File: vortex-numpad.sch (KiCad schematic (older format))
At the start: 16 parts

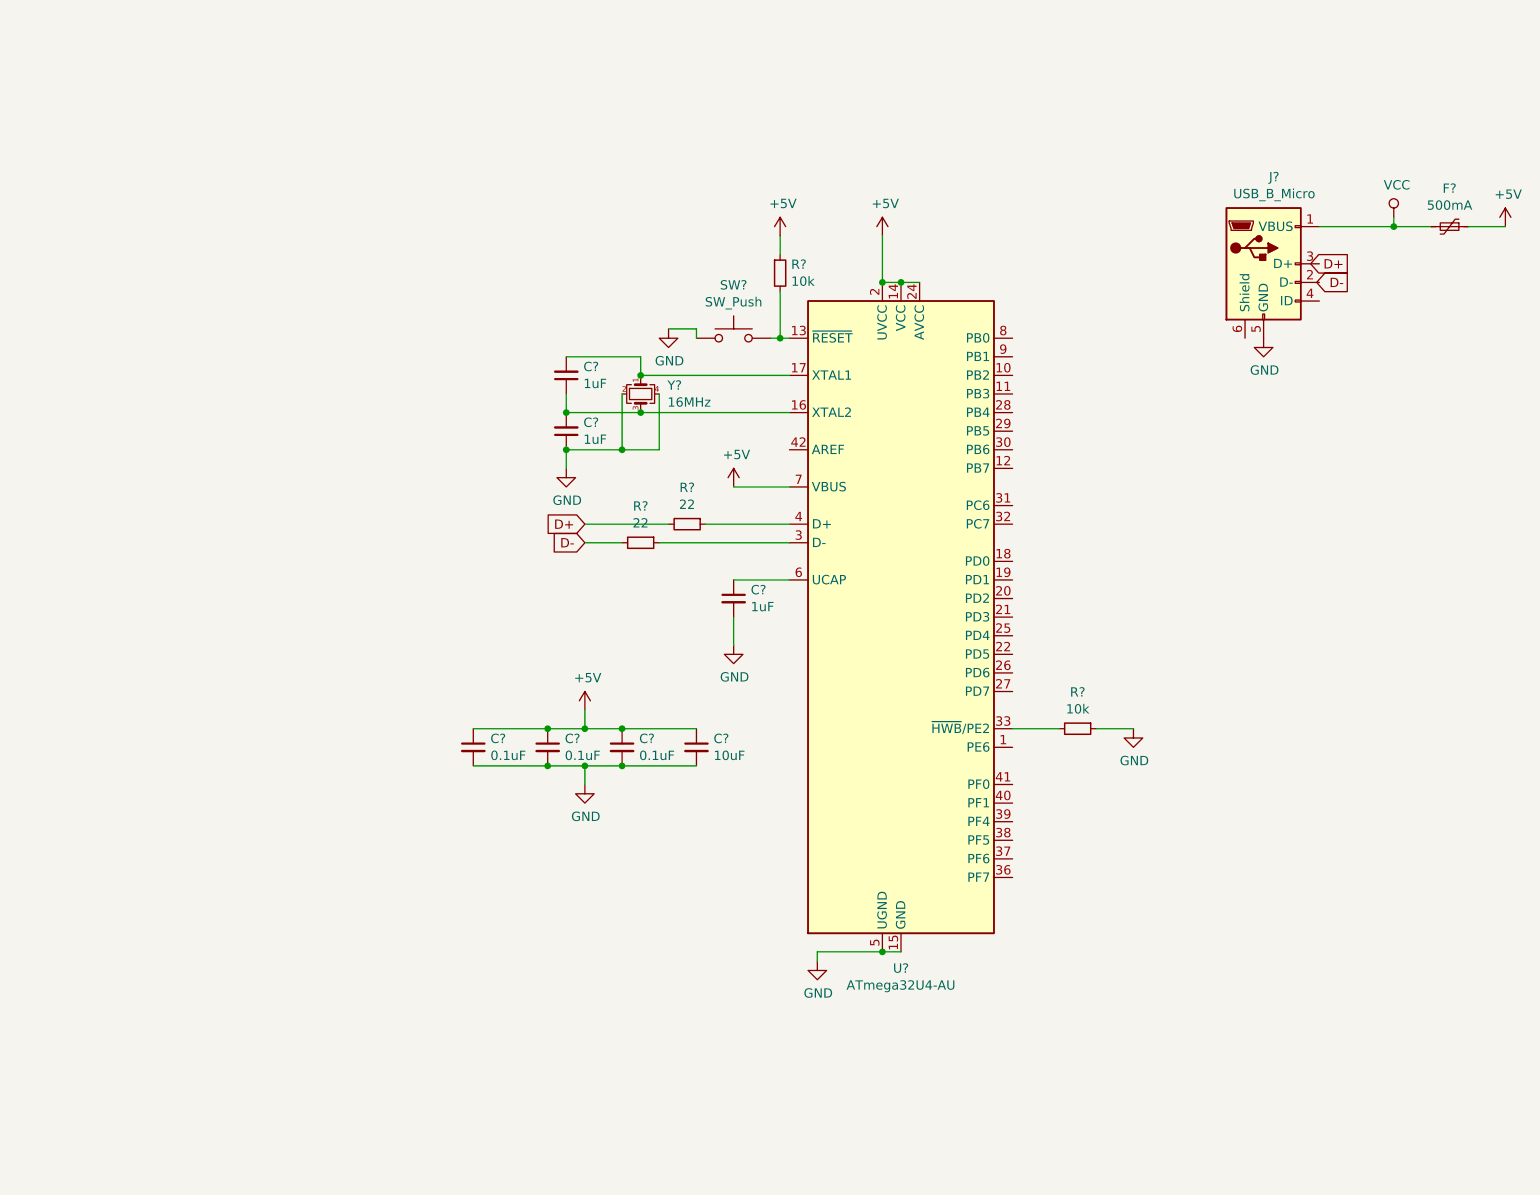
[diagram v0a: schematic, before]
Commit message: Schematic laid out
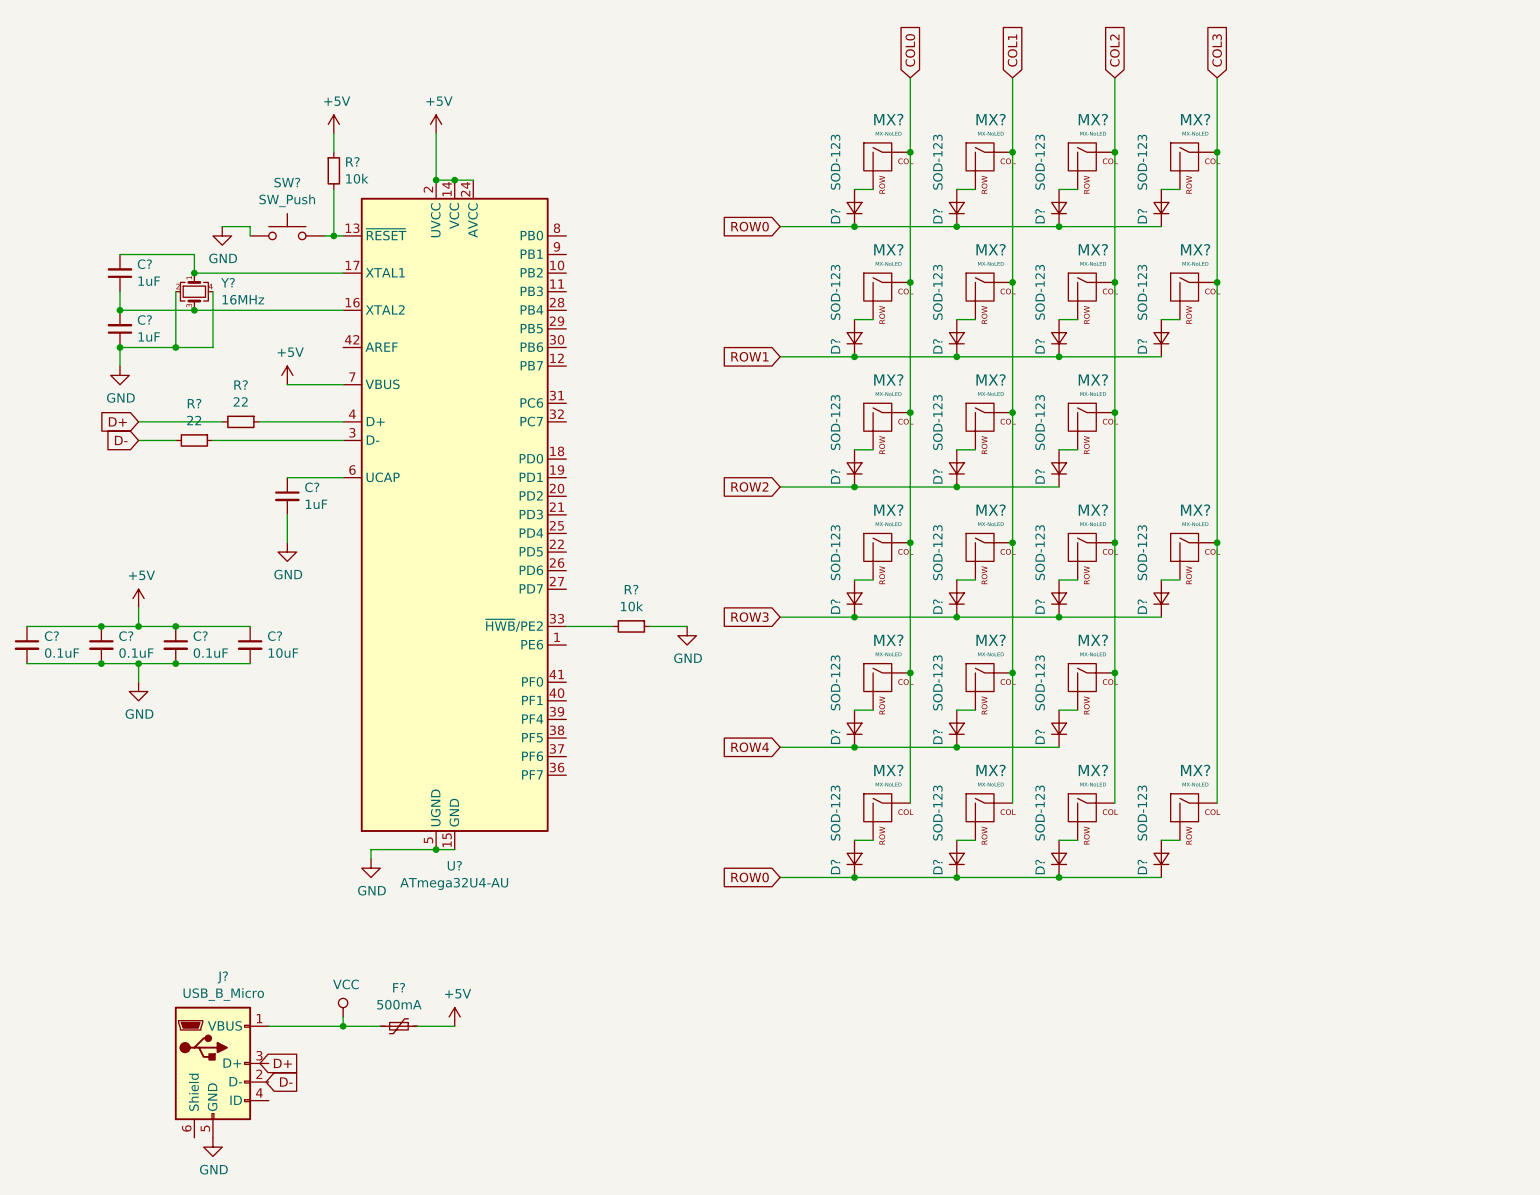
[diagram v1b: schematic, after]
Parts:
- added D? (x22): SOD-123, symbol Device:D_Small
- added MX? (x22): MX-NoLED, symbol MX_Alps_Hybrid:MX-NoLED
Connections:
- new net: D?.2 (A), MX?.2 (ROW) (x22)
- new net COL0: MX?.1 (COL), MX?.1 (COL), MX?.1 (COL), MX?.1 (COL), MX?.1 (COL), MX?.1 (COL)
- new net COL1: MX?.1 (COL), MX?.1 (COL), MX?.1 (COL), MX?.1 (COL), MX?.1 (COL), MX?.1 (COL)
- new net COL2: MX?.1 (COL), MX?.1 (COL), MX?.1 (COL), MX?.1 (COL), MX?.1 (COL), MX?.1 (COL)
- new net COL3: MX?.1 (COL), MX?.1 (COL), MX?.1 (COL), MX?.1 (COL)
- new net ROW0: D?.1 (K), D?.1 (K), D?.1 (K), D?.1 (K), D?.1 (K), D?.1 (K), D?.1 (K), D?.1 (K)
- new net ROW1: D?.1 (K), D?.1 (K), D?.1 (K), D?.1 (K)
- new net ROW2: D?.1 (K), D?.1 (K), D?.1 (K)
- new net ROW3: D?.1 (K), D?.1 (K), D?.1 (K), D?.1 (K)
- new net ROW4: D?.1 (K), D?.1 (K), D?.1 (K)
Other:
- moved on the sheet: C?, F?, J?, R?, SW?, U?, Y?

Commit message: Pins assigned, keys named
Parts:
- gave numbers to parts that had none: 60
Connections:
- net COL0: now also U1.18 (PD0)
- net COL1: now also U1.19 (PD1)
- net COL2: now also U1.20 (PD2)
- net COL3: now also U1.21 (PD3)
- net ROW0: now also U1.32 (PC7); no longer D19.1 (K), D20.1 (K), D21.1 (K), D22.1 (K)
- net ROW1: now also U1.31 (PC6)
- net ROW2: now also U1.30 (PB6)
- net ROW3: now also U1.29 (PB5)
- net ROW4: now also U1.28 (PB4)
- net ROW5: now reaches U1.27 (PD7)
- net ROW5: now also D19.1 (K), D20.1 (K), D21.1 (K), D22.1 (K)

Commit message: Assign footprints
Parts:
- ASTERISK1, FN1, FN2, FN3, FN4, FWDSLASH1, MINUS1, NUM0, NUM1, NUM2, NUM3, NUM4, NUM5, NUM6, NUM7, NUM8, NUM9, NUMDBL0, NUMDOT1, NUMLOCK1, PLUS1, RETURN1: footprint (none) -> MX_Alps_Hybrid:MX-1U-NoLED
- C1, C2, C3, C4, C5, C6, C7, D1, D10, D11, D12, D13, D14, D15, D16, D17, D18, D19, D2, D20, D21, D22, D3, D4, D5, D6, D7, D8, D9: footprint (none) -> Diode_SMD:D_SOD-123
- F1: footprint (none) -> Fuse:Fuse_1206_3216Metric
- J1: footprint (none) -> Connector_USB:USB_Micro-B_Molex-105017-0001
- R1, R2, R3, R4: footprint (none) -> Resistor_SMD:R_0805_2012Metric
- SW1: footprint (none) -> random-keyboard-parts:SKQG-1155865
- Y1: footprint (none) -> Crystal:Crystal_SMD_3225-4Pin_3.2x2.5mm

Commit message: Initial PCB layout
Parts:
- PLUS1, RETURN1: footprint MX_Alps_Hybrid:MX-1U-NoLED -> MX_Alps_Hybrid:MX-2U-ReversedStabilizers-NoLED
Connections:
- net D+: now also J1.3 (D+)
- net D-: now also J1.2 (D-)
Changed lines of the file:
@@
 Wire Wire Line
 	3100 5900 2900 5900
-Text GLabel 2250 6200 0    50   Output ~ 0
+Text GLabel 2100 6200 2    50   Input ~ 0
 D-
-Text GLabel 2250 6100 0    50   Output ~ 0
+Text GLabel 2100 6100 2    50   Input ~ 0
 D+
 $Comp
@@
 F 0 "PLUS1" H 7083 3573 60  0000 C CNN
 F 1 "MX-NoLED" H 7083 3499 20  0000 C CNN
-F 2 "MX_Alps_Hybrid:MX-1U-NoLED" H 6425 3325 60  0001 C CNN
+F 2 "MX_Alps_Hybrid:MX-2U-ReversedStabilizers-NoLED" H 6425 3325 60  0001 C CNN
 F 3 "" H 6425 3325 60  0001 C CNN
 	1    7050 3350
@@
 F 0 "RETURN1" H 7083 4973 60  0000 C CNN
 F 1 "MX-NoLED" H 7083 4899 20  0000 C CNN
-F 2 "MX_Alps_Hybrid:MX-1U-NoLED" H 6425 4725 60  0001 C CNN
+F 2 "MX_Alps_Hybrid:MX-2U-ReversedStabilizers-NoLED" H 6425 4725 60  0001 C CNN
 F 3 "" H 6425 4725 60  0001 C CNN
 	1    7050 4750

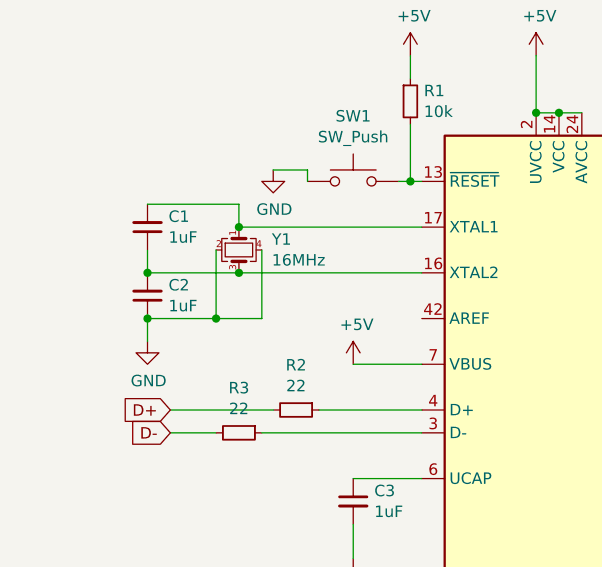
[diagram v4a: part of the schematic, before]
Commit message: Initial traces all done
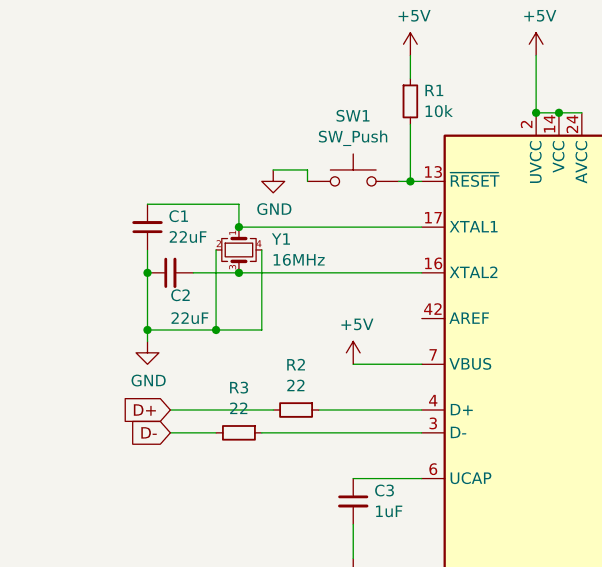
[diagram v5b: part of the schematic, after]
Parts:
- C1, C2: value 1uF -> 22uF
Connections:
- net GND: now also C1.1
- net at C2.2, U1.16 (XTAL2), Y1.3: no longer C1.1
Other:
- moved on the sheet: C2
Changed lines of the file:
@@
-$EndComp
-$Comp
-L Device:C_Small C2
-U 1 1 5D680838
-P 1300 2150
-F 0 "C2" H 1208 2104 50  0000 R CNN
-F 1 "1uF" H 1208 2195 50  0000 R CNN
-F 2 "Diode_SMD:D_SOD-123" H 1300 2150 50  0001 C CNN
-F 3 "~" H 1300 2150 50  0001 C CNN
-	1    1300 2150
-	-1   0    0    1
 $EndComp
 $Comp
@@
 P 1300 1850
 F 0 "C1" H 1208 1804 50  0000 R CNN
-F 1 "1uF" H 1208 1895 50  0000 R CNN
+F 1 "22uF" H 1208 1895 50  0000 R CNN
 F 2 "Diode_SMD:D_SOD-123" H 1300 1850 50  0001 C CNN
 F 3 "~" H 1300 1850 50  0001 C CNN
@@
 Wire Wire Line
 	1300 1950 1300 2050
-Wire Wire Line
-	1300 2050 1700 2050
-Connection ~ 1300 2050
-Connection ~ 1700 2050
-Wire Wire Line
-	1800 1950 1800 2250
-Wire Wire Line
-	1800 2250 1600 2250
-Wire Wire Line
-	1600 1950 1600 2250
-Connection ~ 1600 2250
-Wire Wire Line
-	1600 2250 1300 2250
 $Comp
 L power:GND #PWR0108
@@
 	1    0    0    -1
 $EndComp
-Wire Wire Line
-	1300 2250 1300 2350
-Connection ~ 1300 2250
 $Comp
 L power:GND #PWR0109
@@
 Text GLabel 3700 3150 2    50   Input ~ 0
 COL3
+$Comp
+L Device:C_Small C2
+U 1 1 5D680838
+P 1400 2050
+F 0 "C2" V 1300 2050 50  0000 R CNN
+F 1 "22uF" V 1200 2050 50  0000 R CNN
+F 2 "Diode_SMD:D_SOD-123" H 1400 2050 50  0001 C CNN
+F 3 "~" H 1400 2050 50  0001 C CNN
+	1    1400 2050
+	0    -1   -1   0
+$EndComp
+Wire Wire Line
+	1300 2350 1300 2300
+Wire Wire Line
+	1300 2300 1600 2300
+Wire Wire Line
+	1800 1950 1800 2300
+Wire Wire Line
+	1600 1950 1600 2300
+Connection ~ 1600 2300
+Wire Wire Line
+	1600 2300 1800 2300
+Wire Wire Line
+	1300 2050 1300 2300
+Connection ~ 1300 2050
+Connection ~ 1300 2300
+Wire Wire Line
+	1500 2050 1700 2050
+Connection ~ 1700 2050
 $EndSCHEMATC
